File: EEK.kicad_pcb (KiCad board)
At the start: 2 copper layers, 165 x 51.8 mm, 35 parts

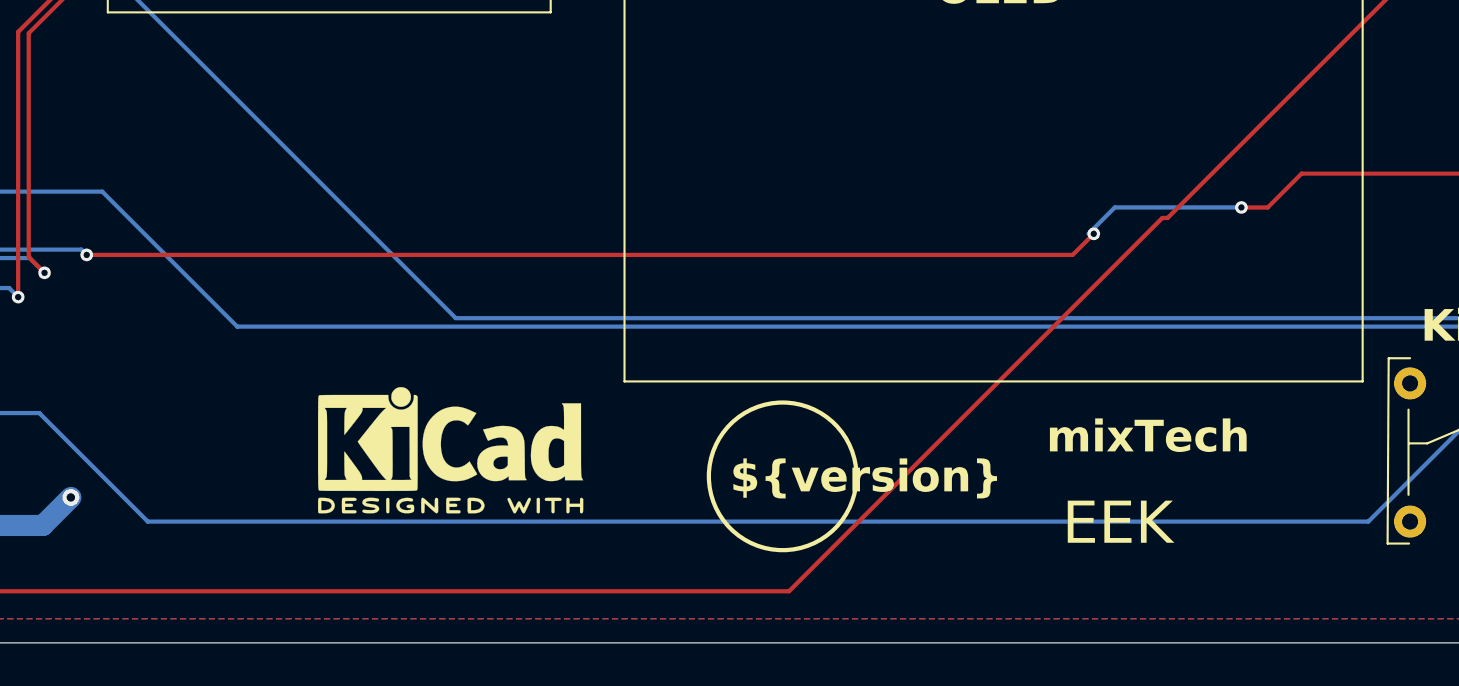
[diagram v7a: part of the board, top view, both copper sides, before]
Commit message: Add 141R mixTech logo
Add 141R mixTech logo
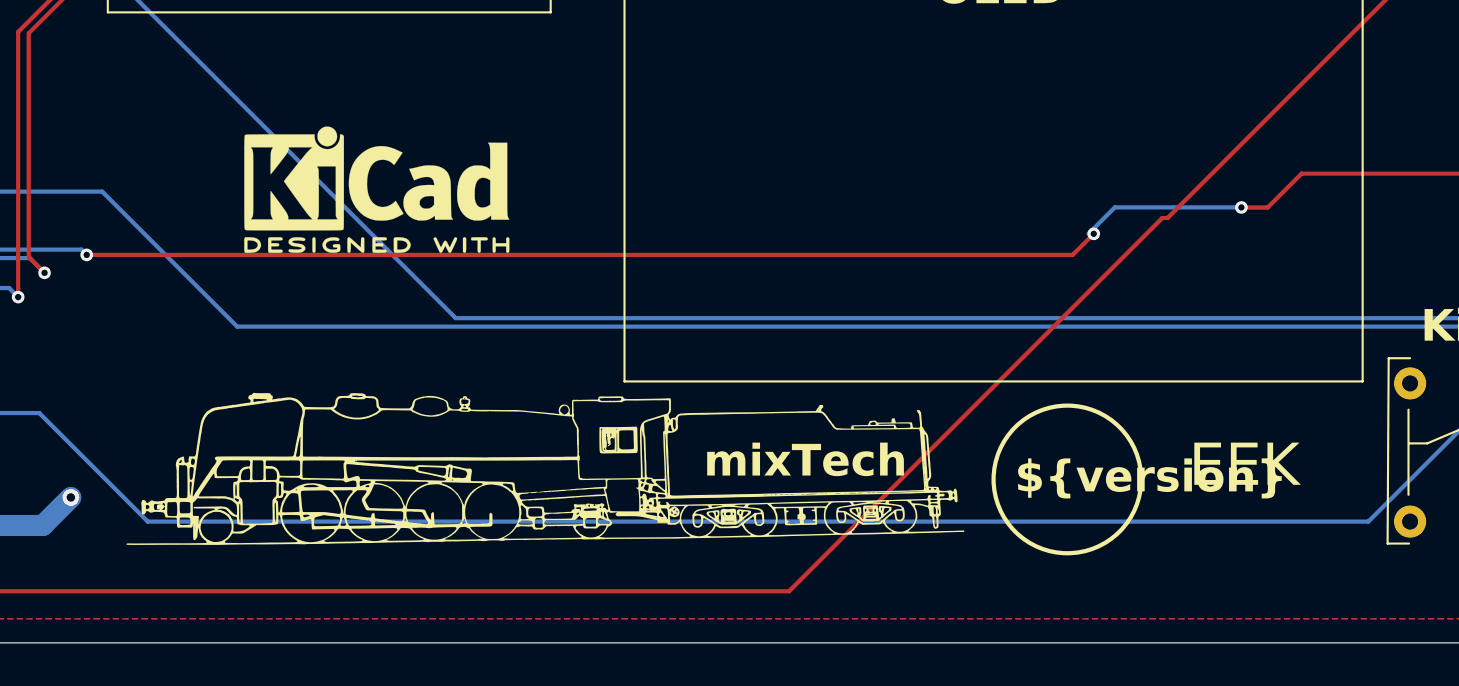
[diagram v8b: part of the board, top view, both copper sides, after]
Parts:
- added G***: LOGO, PH_lib:LOGO mixTech, F.Cu at (137.4, 119.8)
- moved REF** 12.8 mm to (129.5, 107.0)
